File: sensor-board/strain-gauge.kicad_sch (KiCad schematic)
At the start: 4 parts, among them U3 Opamp_Quad

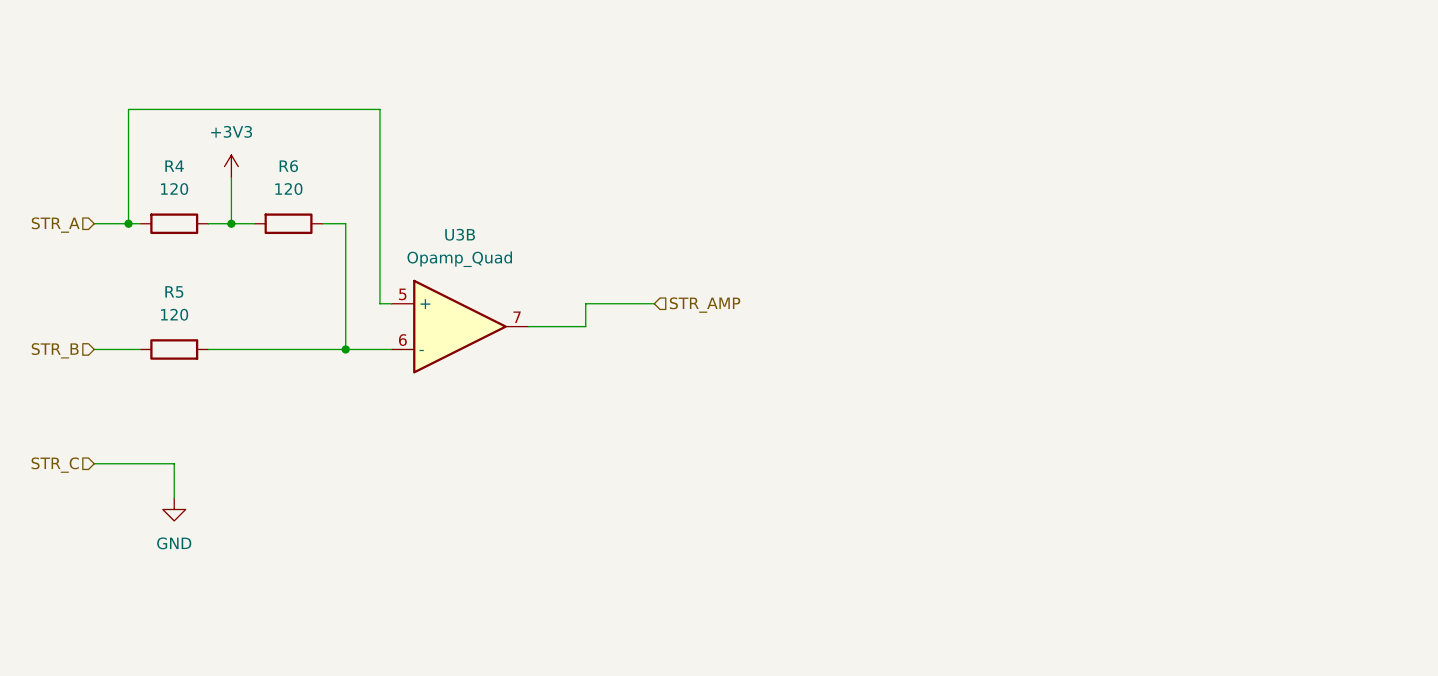
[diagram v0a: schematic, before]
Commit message: Updated main board: replace quad-channel op amps with single-channel instrumentation amps and wheatstone bridge (as per breakout board)
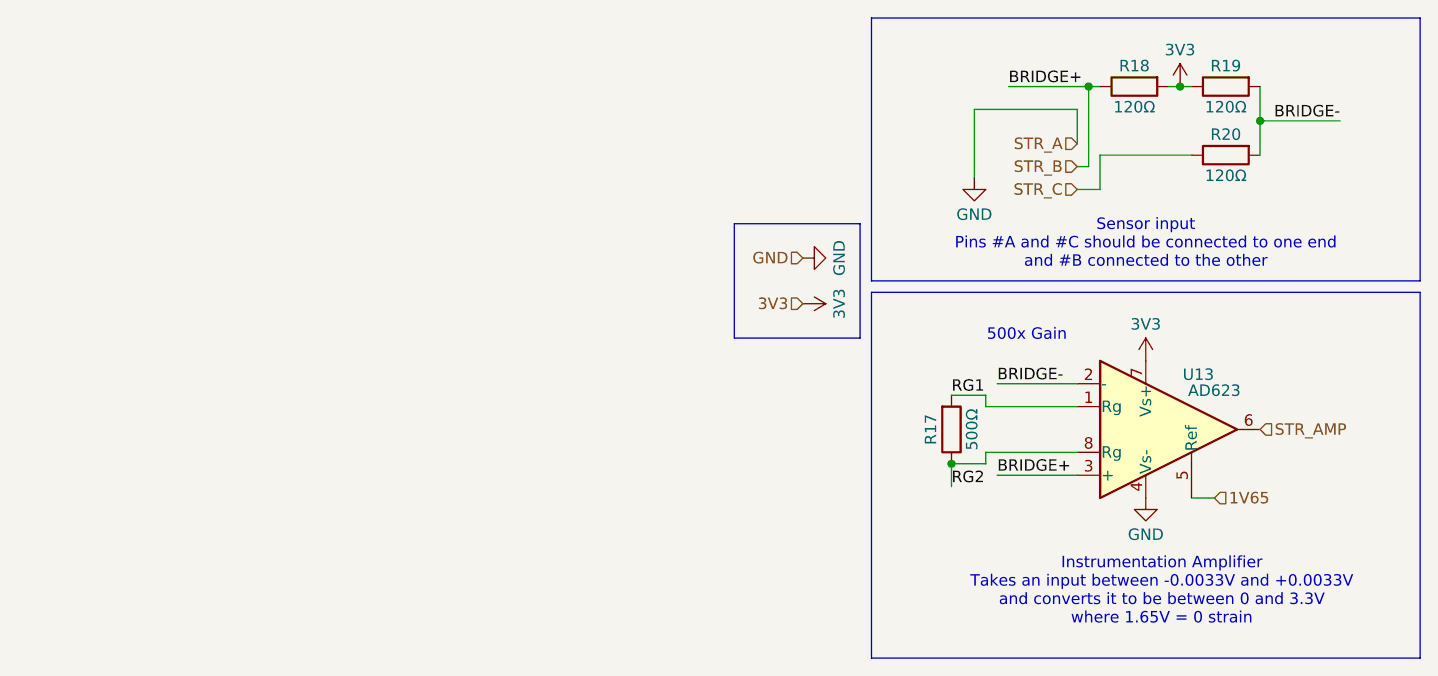
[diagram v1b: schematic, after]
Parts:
- removed R4, R5, R6: 120, Resistor_SMD:R_0805_2012Metric, symbol Device:R
- removed U3: Opamp_Quad, Package_SO:SO-14_3.9x8.65mm_P1.27mm, symbol Device:Opamp_Quad
- added R17: 500Ω, Resistor_SMD:R_0805_2012Metric, symbol Device:R
- added R18, R19, R20: 120Ω, Resistor_SMD:R_0805_2012Metric, symbol Device:R
- added U13: AD623, Package_SO:MSOP-8_3x3mm_P0.65mm, symbol Amplifier_Instrumentation:AD623
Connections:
- net GND: now also U13.4 (Vs-)
- net STR_AMP: now also U13.6
- net STR_B: now also R18.1, U13.3 (+)
- new net 1V65: U13.5 (Ref)
- new net 3V3: R18.2, R19.1, U13.7 (Vs+)
- new net BRIDGE-: R19.2, R20.2, U13.2 (-)
- new net RG1: R17.2, U13.1 (Rg)
- new net RG2: R17.1, U13.8 (Rg)
- new net STR_C: R20.1
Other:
- note added: "500x Gain"
- note added: "Instrumentation Amplifier Takes an input between -0.0033V and +0.0033V and converts it to be between 0 and 3.3V where 1.65V = 0 strain"
- note added: "Sensor input Pins #A and #C should be connected to one end and #B connected to the other"

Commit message: WIP
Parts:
- R17, R18, R19, R20: footprint Resistor_SMD:R_0805_2012Metric -> Resistor_SMD:R_0603_1608Metric
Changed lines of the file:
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@@
 	(label "BRIDGE+"
 		(at 151.13 92.71 0)
-		(fields_autoplaced yes)
 		(effects
 			(font
@@
 	(label "BRIDGE-"
 		(at 189.23 53.34 180)
-		(fields_autoplaced yes)
 		(effects
 			(font
@@
 	(label "RG2"
 		(at 146.05 93.98 0)
-		(fields_autoplaced yes)
 		(effects
 			(font
@@
 	(label "BRIDGE+"
 		(at 152.4 49.53 0)
-		(fields_autoplaced yes)
 		(effects
 			(font
@@
 	(label "RG1"
 		(at 146.05 83.82 0)
-		(fields_autoplaced yes)
 		(effects
 			(font
@@
 	(label "BRIDGE-"
 		(at 151.13 82.55 0)
-		(fields_autoplaced yes)
 		(effects
 			(font
@@
 		(shape input)
 		(at 175.26 95.25 0)
-		(fields_autoplaced yes)
 		(effects
 			(font
@@
 		(shape input)
 		(at 180.34 87.63 0)
-		(fields_autoplaced yes)
 		(effects
 			(font
@@
 		(shape input)
 		(at 160.02 55.88 180)
-		(fields_autoplaced yes)
 		(effects
 			(font
@@
 		(shape input)
 		(at 160.02 58.42 180)
-		(fields_autoplaced yes)
 		(effects
 			(font
@@
 		(shape input)
 		(at 129.54 73.66 180)
-		(fields_autoplaced yes)
 		(effects
 			(font
@@
 		(shape input)
 		(at 160.02 60.96 180)
-		(fields_autoplaced yes)
 		(effects
 			(font
@@
 		(shape input)
 		(at 129.54 68.58 180)
-		(fields_autoplaced yes)
 		(effects
 			(font
@@
 			)
 		)
-		(property "Footprint" "Resistor_SMD:R_0805_2012Metric"
+		(property "Footprint" "Resistor_SMD:R_0603_1608Metric"
 			(at 144.272 87.63 90)
 			(effects
@@
 			)
 		)
-		(property "Footprint" "Resistor_SMD:R_0805_2012Metric"
+		(property "Footprint" "Resistor_SMD:R_0603_1608Metric"
 			(at 166.37 47.752 90)
 			(effects
@@
 			)
 		)
-		(property "Footprint" "Resistor_SMD:R_0805_2012Metric"
+		(property "Footprint" "Resistor_SMD:R_0603_1608Metric"
 			(at 176.53 55.372 90)
 			(effects
@@
 			)
 		)
-		(property "Footprint" "Resistor_SMD:R_0805_2012Metric"
+		(property "Footprint" "Resistor_SMD:R_0603_1608Metric"
 			(at 176.53 47.752 90)
 			(effects

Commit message: Please unbreak the schematic
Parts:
- removed R17: 500Ω, Resistor_SMD:R_0603_1608Metric, symbol Device:R
- removed R18, R19, R20: 120Ω, Resistor_SMD:R_0603_1608Metric, symbol Device:R
- removed U13: AD623, Package_SO:MSOP-8_3x3mm_P0.65mm, symbol Amplifier_Instrumentation:AD623
- added R4, R5, R6: 120, Resistor_SMD:R_0805_2012Metric, symbol Device:R
- added U3: Opamp_Quad, Package_SO:SO-14_3.9x8.65mm_P1.27mm, symbol Device:Opamp_Quad
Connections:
- net STR_AMP: now also U3.7
- net STR_B: now also R5.1
- new net: R5.2, R6.1, U3.6 (-)
- new net +3V3: R4.1, R6.2
- new net STR_A: R4.2, U3.5 (+)
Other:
- note removed: "500x Gain"
- note removed: "Instrumentation Amplifier Takes an input between -0.0033V and +0.0033V and converts it to be between 0 and 3.3V where 1.65V = 0 strain"
- note removed: "Sensor input Pins #A and #C should be connected to one end and #B connected to the other"

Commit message: fixing schematic implosion
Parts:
- removed R4, R5, R6: 120, Resistor_SMD:R_0805_2012Metric, symbol Device:R
- removed U3: Opamp_Quad, Package_SO:SO-14_3.9x8.65mm_P1.27mm, symbol Device:Opamp_Quad
- added R17: 500Ω, Resistor_SMD:R_0603_1608Metric, symbol Device:R
- added R18, R19, R20: 120Ω, Resistor_SMD:R_0603_1608Metric, symbol Device:R
- added U13: AD623, Package_SO:MSOP-8_3x3mm_P0.65mm, symbol Amplifier_Instrumentation:AD623
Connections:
- net GND: now also U13.4 (Vs-)
- net STR_AMP: now also U13.6
- net STR_B: now also R18.1, U13.3 (+)
- new net 1V65: U13.5 (Ref)
- new net 3V3: R18.2, R19.1, U13.7 (Vs+)
- new net BRIDGE-: R19.2, R20.2, U13.2 (-)
- new net RG1: R17.2, U13.1 (Rg)
- new net RG2: R17.1, U13.8 (Rg)
- new net STR_C: R20.1
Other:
- note added: "500x Gain"
- note added: "Instrumentation Amplifier Takes an input between -0.0033V and +0.0033V and converts it to be between 0 and 3.3V where 1.65V = 0 strain"
- note added: "Sensor input Pins #A and #C should be connected to one end and #B connected to the other"

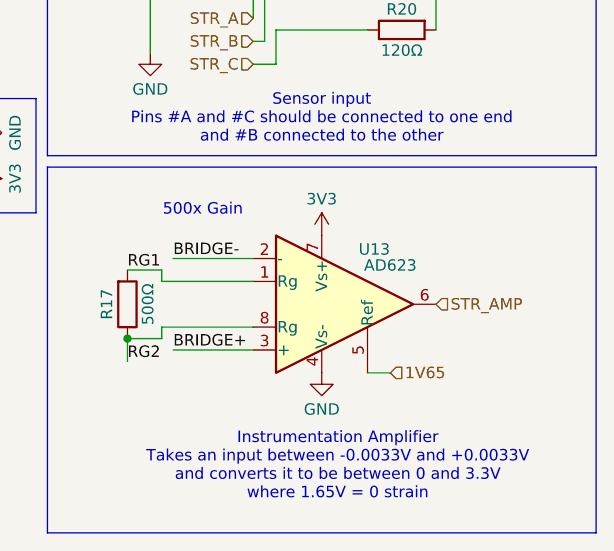
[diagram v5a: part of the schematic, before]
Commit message: add sensor board
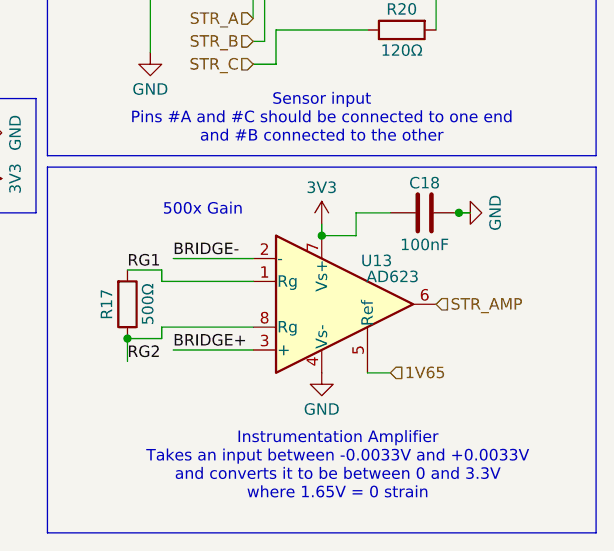
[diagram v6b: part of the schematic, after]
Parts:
- added C18: 100nF, Capacitor_SMD:C_0603_1608Metric, symbol Device:C
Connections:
- net 3V3: now also C18.2
- net GND: now also C18.1

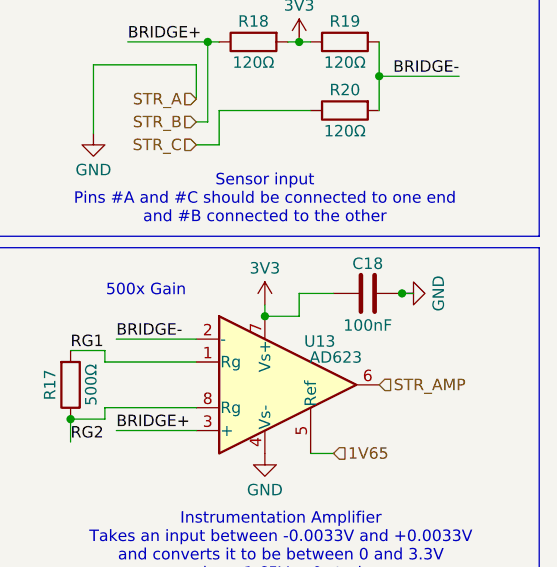
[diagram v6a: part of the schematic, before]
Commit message: Add decoupling caps and re-layout board
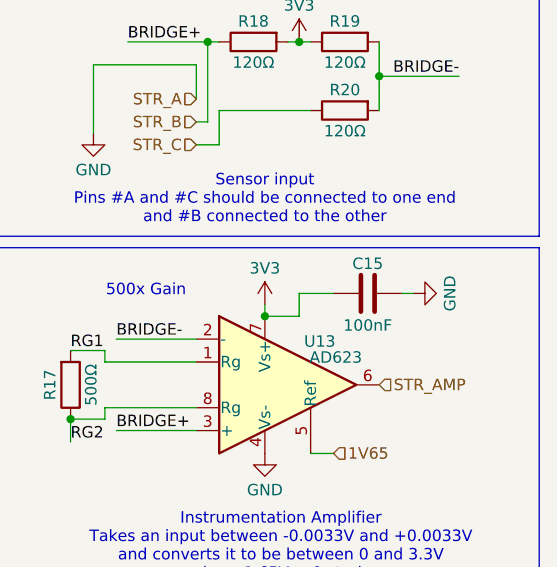
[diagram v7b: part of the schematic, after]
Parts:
- renumbered C18 to C15
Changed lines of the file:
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@@
-	)
-	(junction
-		(at 182.88 77.47)
-		(diameter 0)
-		(color 0 0 0 0)
 	)
 	(junction
@@
 	(wire
 		(pts
-			(xy 182.88 77.47) (xy 184.15 77.47)
-		)
-		(stroke
-			(width 0)
-			(type default)
-		)
-	)
-	(wire
-		(pts
 			(xy 162.56 60.96) (xy 160.02 60.96)
 		)
@@
 		(pts
 			(xy 180.34 49.53) (xy 180.34 53.34)
+		)
+		(stroke
+			(width 0)
+			(type default)
+		)
+	)
+	(wire
+		(pts
+			(xy 184.15 77.47) (xy 182.88 77.47)
 		)
 		(stroke
@@
 		(on_board yes)
 		(dnp no)
-		(property "Reference" "C18"
+		(property "Reference" "C15"
 			(at 179.07 74.168 90)
 			(effects
@@
 	(symbol
 		(lib_id "power:GND")
-		(at 182.88 77.47 90)
+		(at 184.15 77.47 90)
 		(mirror x)
 		(unit 1)
@@
 		(on_board yes)
 		(dnp no)
-		(property "Reference" "#PWR0120"
-			(at 189.23 77.47 0)
+		(property "Reference" "#PWR0133"
+			(at 190.5 77.47 0)
 			(effects
 				(font
@@
 		)
 		(property "Value" "GND"
-			(at 186.944 77.47 0)
+			(at 188.214 77.47 0)
 			(effects
 				(font
@@
 		)
 		(property "Footprint" ""
-			(at 182.88 77.47 0)
+			(at 184.15 77.47 0)
 			(effects
 				(font
@@
 		)
 		(property "Datasheet" ""
-			(at 182.88 77.47 0)
+			(at 184.15 77.47 0)
 			(effects
 				(font
@@
 		)
 		(property "Description" "Power symbol creates a global label with name \"GND\" , ground"
-			(at 182.88 77.47 0)
+			(at 184.15 77.47 0)
 			(effects
 				(font
@@
 		)
 	)
+	(sheet_instances
+		(path "/"
+			(page "1")
+		)
+	)
